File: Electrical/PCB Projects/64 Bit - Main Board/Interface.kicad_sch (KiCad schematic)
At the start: 13 parts, among them U7 EN12-VS20AF20

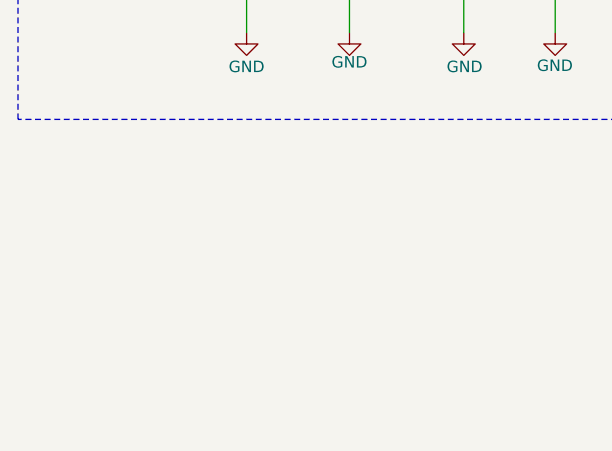
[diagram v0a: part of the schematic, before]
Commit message: finished routing - added photoresistor to analog pin. Updated STM32Cube setup. Final stages of hardware design
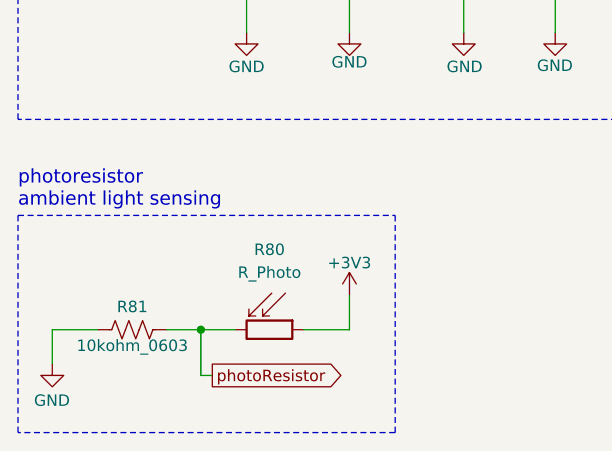
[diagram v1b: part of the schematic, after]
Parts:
- added R80: R_Photo, OptoDevice:R_LDR_5.1x4.3mm_P3.4mm_Vertical, symbol Device:R_Photo
- added R81: 10kohm_0603, Resistor_SMD:R_0603_1608Metric, symbol Device:R_US
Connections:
- net +3V3: now also R80.1
- net GND: now also R81.1
- new net photoResistor: R80.2, R81.2
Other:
- note added: "photoresistor ambient light sensing"

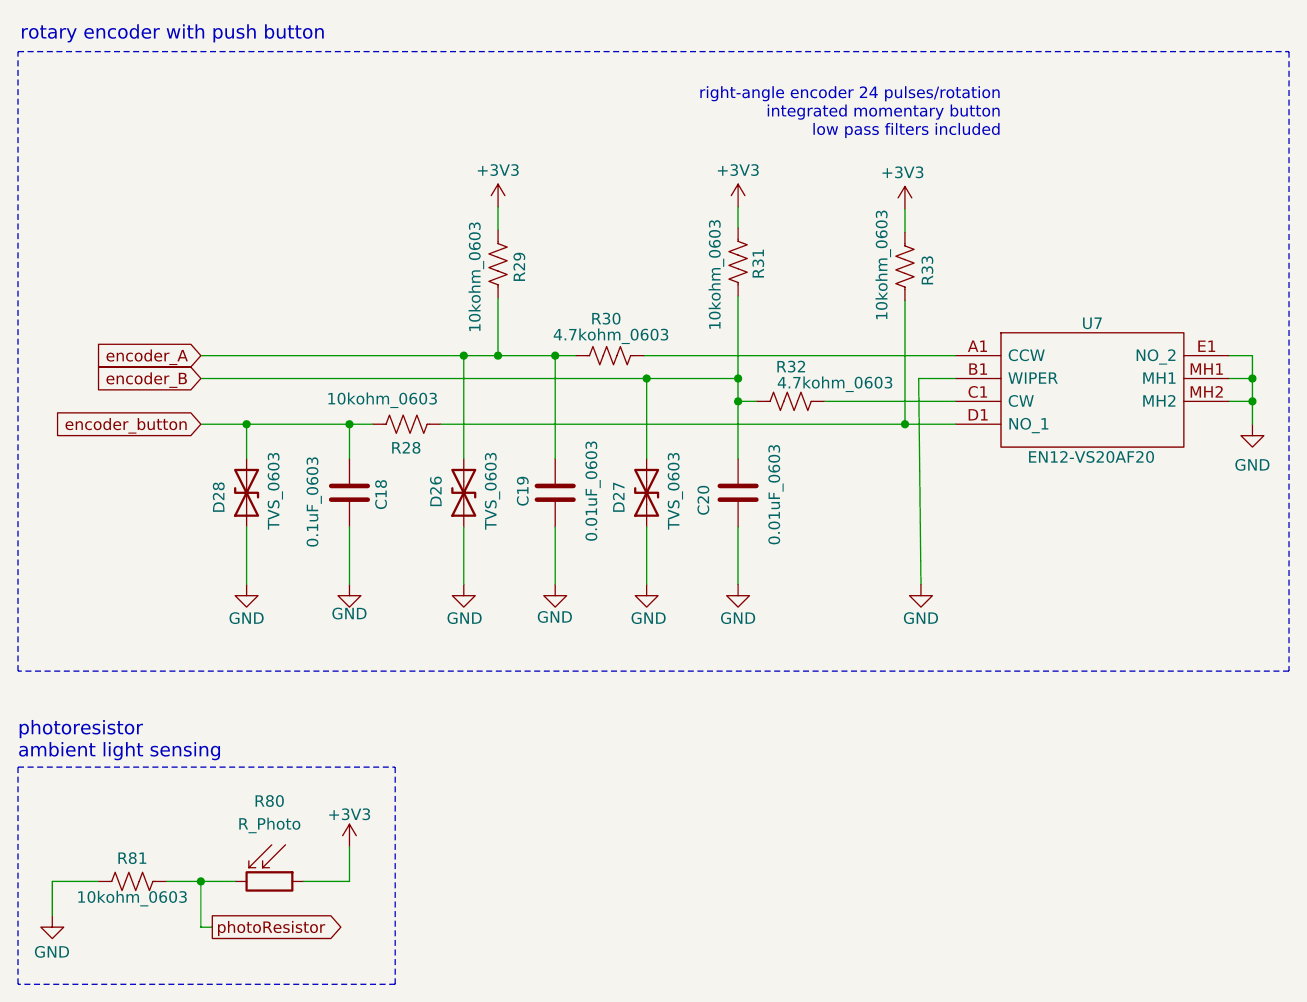
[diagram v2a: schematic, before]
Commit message: final. PCB outputs generated, ordering prototypes
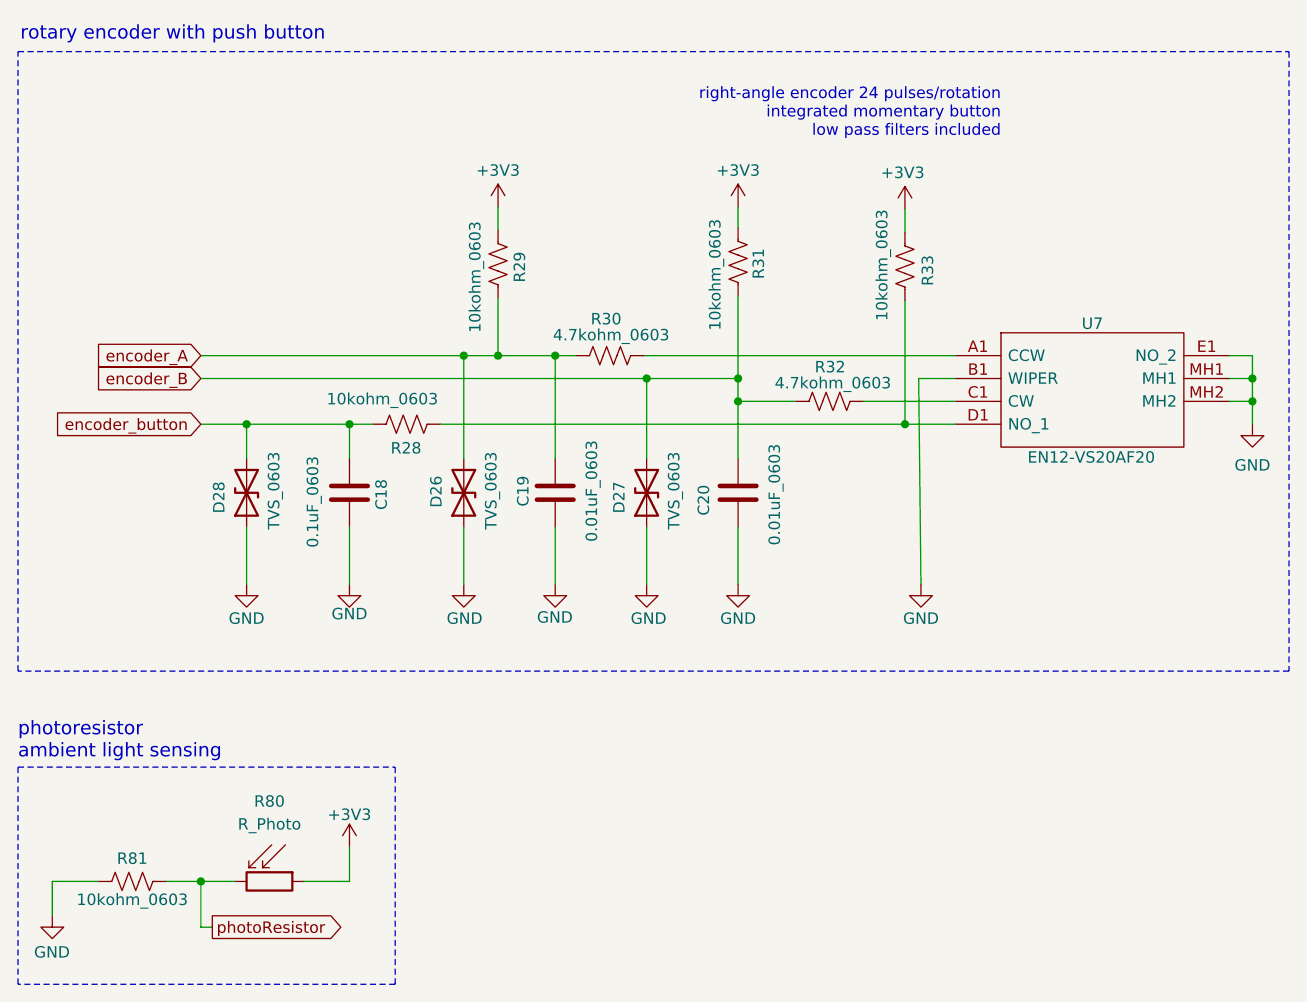
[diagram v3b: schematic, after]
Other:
- moved on the sheet: R32
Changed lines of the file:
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@@
 	(wire
 		(pts
-			(xy 154.94 101.6) (xy 156.972 101.6)
+			(xy 154.94 101.6) (xy 161.29 101.6)
 		)
 		(stroke
@@
 	(wire
 		(pts
-			(xy 164.592 101.6) (xy 179.07 101.6)
+			(xy 168.91 101.6) (xy 179.07 101.6)
 		)
 		(stroke
@@
 		)
 		(property "Value" "10kohm_0603"
-			(at 87.63 156.718 90)
+			(at 87.63 156.972 90)
 			(effects
 				(font
@@
 	(symbol
 		(lib_id "Device:R_US")
-		(at 160.782 101.6 90)
+		(at 165.1 101.6 90)
 		(unit 1)
 		(exclude_from_sim no)
@@
 		(dnp no)
 		(property "Reference" "R32"
-			(at 162.56 97.79 90)
+			(at 166.878 97.79 90)
 			(effects
 				(font
@@
 		)
 		(property "Value" "4.7kohm_0603"
-			(at 172.212 99.568 90)
+			(at 171.958 99.568 90)
 			(effects
 				(font
@@
 		)
 		(property "Footprint" "Resistor_SMD:R_0603_1608Metric"
-			(at 161.036 100.584 90)
+			(at 165.354 100.584 90)
 			(effects
 				(font
@@
 		)
 		(property "Datasheet" "~"
-			(at 160.782 101.6 0)
+			(at 165.1 101.6 0)
 			(effects
 				(font
@@
 		)
 		(property "Description" ""
-			(at 160.782 101.6 0)
+			(at 165.1 101.6 0)
 			(effects
 				(font
